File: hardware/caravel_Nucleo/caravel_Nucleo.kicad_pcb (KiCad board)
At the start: 2 copper layers, 67 x 92.4 mm, 80 parts, among them J1 USB_B_Micro - 10118193-0001LF, J10 Conn_01x09_Female, J2 Conn_01x02_Female, J3 Conn_01x02_Male, J4 Conn_01x04_Female, J5 Conn_01x02_Male, J6 Conn_01x02_Male, J7 Conn_01x06_Female, J8 Conn_01x03, J9 Conn_01x03, SW1 SW_Push - SKQGADE010, T1 Logo, T2 Logo, U1 FT232H, U10 MCP4661, U11 NUCLEO144-F429ZI, U2 SN74LVC1G125DCKR, U3 SN74LVC1G125DCKR, U4 MCP1319MT-29LE-OT, U5 TAR5SxxU_SOT353F, U6 TAR5SxxU_SOT353F, U7 W25Q32FVSS, U8 caravel_breakout, U9 MIC2211-AAYML-TR, X1 DSC6001_10MHZ, Y1 CSTNE12M0GH5L000R0

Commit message: [in review] update caravel board Nucleo-144 hat
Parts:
- added J11: Conn_01x03, Connector_PinHeader_2.54mm:PinHeader_1x03_P2.54mm_Vertical, F.Cu at (146.9, 123.0)
- moved T2 52.3 mm to (109.0, 144.6)
- moved T1 51.8 mm to (109.0, 149.0)
- moved J5 3.95 mm to (108.7, 95.3), turned to 0 degrees
- moved D4 3.37 mm to (119.9, 151.3)
- moved R14 3.37 mm to (124.2, 151.3)
- moved J9 1.77 mm to (108.7, 89.9)
- moved X1 1.29 mm to (150.8, 104.9)
- moved J6 1.29 mm to (146.2, 104.9)
- moved J3 0.51 mm to (148.3, 138.7)
- moved D1 0.51 mm to (141.4, 98.2)
- moved D2 0.51 mm to (138.9, 98.2)
- moved R5 0.41 mm to (153.5, 74.7)
- moved R6 0.41 mm to (151.4, 74.7)
- moved C3 0.28 mm to (152.0, 91.3)
- moved C2 0.28 mm to (151.9, 89.1)
- renumbered R12 to R11, R13 to R12, R11 to R13
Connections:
- J10 pad 9: TIM3_CH2 -> xclk
- J3 pad 2: vccd1 -> vccd
- J4 pad 2: UART3_TX -> UART8_TX
- J4 pad 3: UART3_RX -> UART8_RX
- J5 pad 2: vddio -> vdda
- U1 pad 13: USB_SCK_TXD -> SPI5_SCK
- U1 pad 14: USB_SO_RXD -> SPI5_MISO
- U1 pad 15: USB_SI -> SPI5_MOSI
- U1 pad 16: USB_CS1 -> SPI5_CS
- U11 pad 1: UART3_TX -> unconnected-(U11-Pad1)
- U11 pad 136: unconnected-(U11-Pad136) -> UART8_RX
- U11 pad 2: UART3_RX -> unconnected-(U11-Pad2)
- U11 pad 29: unconnected-(U11-Pad29) -> PH0
- U11 pad 61: unconnected-(U11-Pad61) -> UART8_TX
- U2 pad 2: UART3_RX -> UART8_RX
- U2 pad 4: USB_SO_RXD -> SPI5_MISO
- U3 pad 2: USB_SCK_TXD -> SPI5_SCK
- U3 pad 4: UART3_TX -> UART8_TX
- U8 pad 36: UART3_RX -> UART8_RX
- U8 pad 37: UART3_TX -> UART8_TX
- U8 pad 38: USB_SCK_TXD -> SPI5_SCK
- U8 pad 39: USB_CS1 -> SPI5_CS
- U8 pad 40: USB_SO_RXD -> SPI5_MISO
- U8 pad 41: USB_SI -> SPI5_MOSI
- U8 pad 43: vccd1 -> vccd
- U8 pad 52: TIM3_CH2 -> xclk
- U8 pad 55: vddio -> vdda
- U8 pad 7: vddio -> vdda
- X1 pad 3: TIM3_CH2 -> xclk
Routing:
- net vdda: track 125.8 -> 328.0 mm, vias 8 -> 19
- net vccd: track 0.00 -> 142.7 mm, vias 0 -> 6
- net UART8_RX: track 0.00 -> 140.3 mm, vias 0 -> 5
- net SPI5_SCK: track 0.00 -> 132.6 mm, vias 0 -> 5
- net ~{RST}: track 15.6 -> 146.6 mm, vias 0 -> 2
- net SPI5_MISO: track 0.00 -> 130.2 mm, vias 0 -> 6
- net UART8_TX: track 0.00 -> 129.5 mm, vias 0 -> 5
- net GND: track 54.1 -> 174.2 mm, vias 9 -> 38
- net SPI5_CS: track 0.00 -> 114.8 mm, vias 0 -> 4
- net SPI5_MOSI: track 0.00 -> 99.4 mm, vias 0 -> 3
- net mprj_io[29]: track 0.00 -> 75.3 mm, vias 0 -> 2
- net mprj_io[28]: track 0.00 -> 73.7 mm
- net xclk: track 0.00 -> 71.9 mm, vias 0 -> 3
- net mprj_io[31]: track 0.00 -> 71.9 mm, vias 0 -> 2
- net mprj_io[30]: track 0.00 -> 70.1 mm, vias 0 -> 2
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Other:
- board size 67 x 92.4 mm -> 68.1 x 92.5 mm
- board text added: "5V"
- board text added: "CSB"
- board text added: "D0"
- board text added: "D1"
- board text added: "HAT"
- board text added: "IO[0]"
- board text added: "IO[10]"
- board text added: "IO[11]"
- board text added: "IO[12]"
- board text added: "IO[13]"
- board text added: "IO[14]"
- board text added: "IO[15]"
- board text added: "IO[16]"
- board text added: "IO[17]"
- board text added: "IO[18]"
- board text added: "IO[19]"
- board text added: "IO[1]"
- board text added: "IO[20]"
- board text added: "IO[21]"
- board text added: "IO[22]"
- board text added: "IO[23]"
- board text added: "IO[24]"
- board text added: "IO[25]"
- board text added: "IO[26]"
- board text added: "IO[27]"
- board text added: "IO[28]"
- board text added: "IO[29]"
- board text added: "IO[2]"
- board text added: "IO[30]"
- board text added: "IO[31]"
- board text added: "IO[32]"
- board text added: "IO[33]"
- board text added: "IO[34]"
- board text added: "IO[35]"
- board text added: "IO[36]"
- board text added: "IO[37]"
- board text added: "IO[3]"
- board text added: "IO[4]"
- board text added: "IO[5]"
- board text added: "IO[6]"
- board text added: "IO[7]"
- board text added: "IO[8]"
- board text added: "IO[9]"
- board text added: "MAIN"
- board text added: "MCO_8MHz"
- board text added: "N"
- board text added: "PH0"
- board text added: "SCL"
- board text added: "SDA"
- board text added: "TIM3_2"
- board text added: "TIM3_PWM"

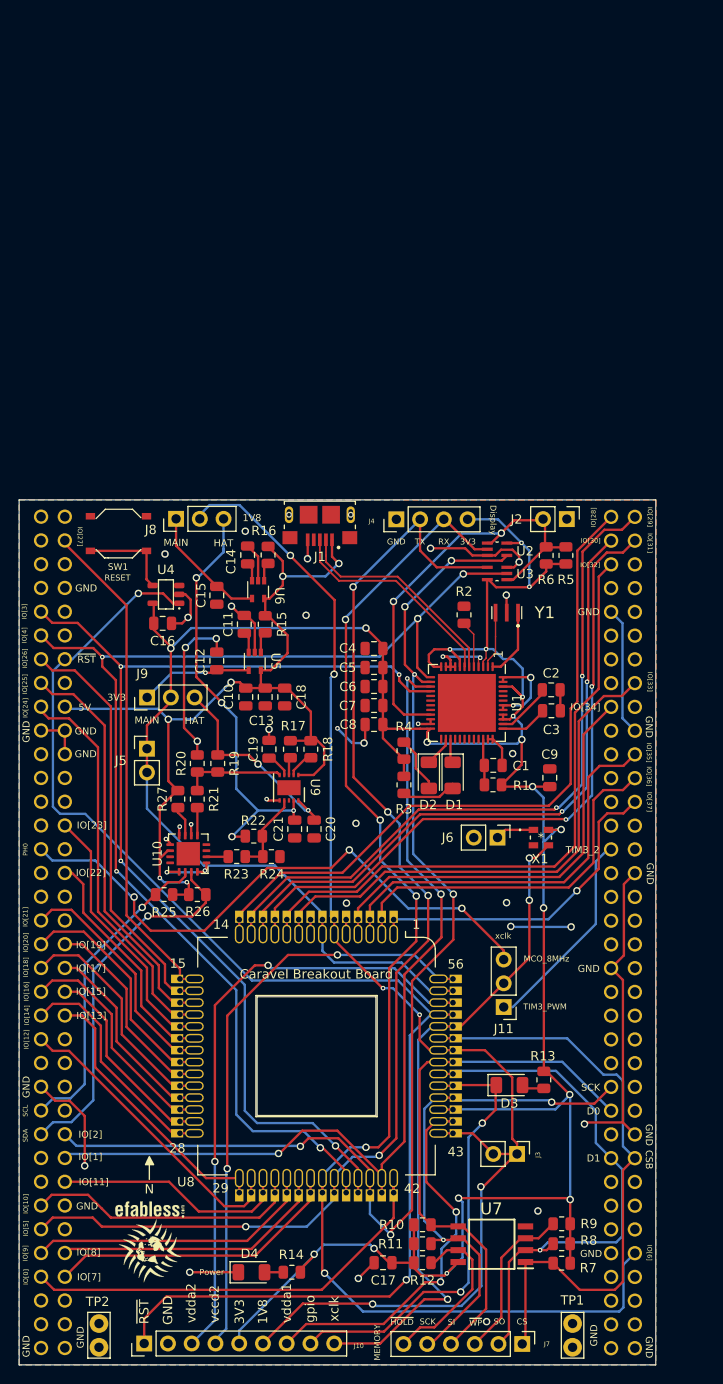
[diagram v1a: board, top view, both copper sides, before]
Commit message: update caravel board Nucleo-144 hat
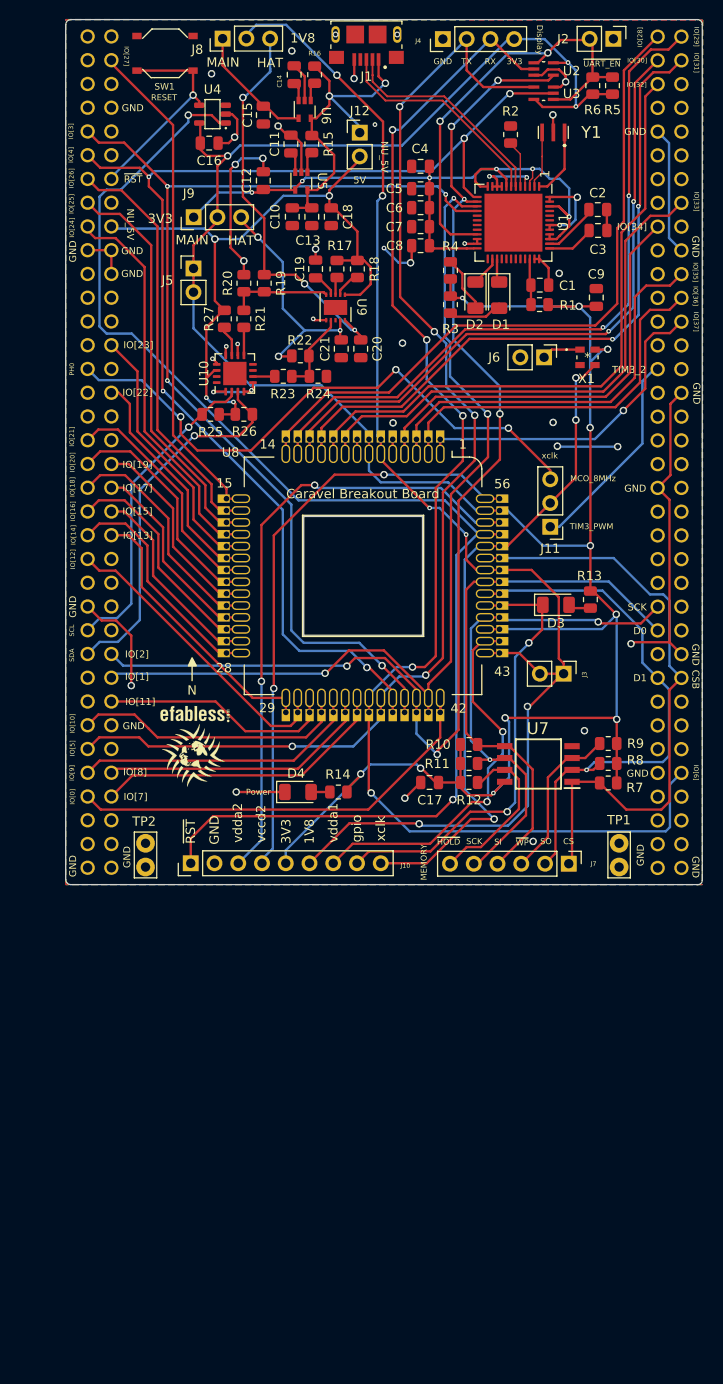
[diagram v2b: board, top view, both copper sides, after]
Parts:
- added J12: Conn_01x02_Male, Connector_PinHeader_2.54mm:PinHeader_1x02_P2.54mm_Vertical, F.Cu at (131.5, 29.5)
- moved T2 53.2 mm to (113.8, 91.6)
- moved T1 53.2 mm to (113.6, 96.1)
- moved C4 51.8 mm to (138.0, 33.1)
- moved R12 51.6 mm to (143.2, 99.0)
- moved C13 51.6 mm to (126.3, 38.5)
- moved C17 51.6 mm to (138.9, 99.0)
- moved C18 51.6 mm to (128.4, 38.5)
- moved D3 51.6 mm to (152.5, 80.0)
- moved J10 51.6 mm to (113.4, 107.6)
- moved U7 51.6 mm to (150.6, 97.0)
- moved C10 51.6 mm to (124.3, 38.5)
- moved C15 51.6 mm to (121.2, 27.6)
- moved C20 51.6 mm to (131.6, 52.6)
- moved C21 51.6 mm to (129.5, 52.6)
- moved J1 51.6 mm to (132.2, 19.0)
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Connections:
- net UART_EN renamed ~{UART_EN}
- C18 pad 2: +5V -> NU_5V
- C4 pad 2: vdda -> V3.3
- C5 pad 2: vdda -> V3.3
- C6 pad 2: vdda -> V3.3
- C7 pad 2: vdda -> V3.3
- C8 pad 2: vdda -> V3.3
- J8 pad 3: VOUT2 -> VOUT1
- J9 pad 3: VOUT1 -> VOUT2
- R17 pad 2: +5V -> NU_5V
- R18 pad 2: +5V -> NU_5V
- R25 pad 1: +5V -> NU_5V
- R26 pad 1: +5V -> NU_5V
- R27 pad 2: +5V -> NU_5V
- U1 pad 12: vdda -> V3.3
- U1 pad 24: vdda -> V3.3
- U1 pad 3: vdda -> V3.3
- U1 pad 39: vdda -> V3.3
- U1 pad 40: vdda -> V3.3
- U1 pad 46: vdda -> V3.3
- U1 pad 8: vdda -> V3.3
- U10 pad 14: +5V -> NU_5V
- U11 pad 14: ~{RST} -> ~{MR}
- U11 pad 18: +5V -> NU_5V
- U9 pad 1: +5V -> NU_5V
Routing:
- net NU_5V: track 0.00 -> 74.5 mm, vias 0 -> 4
- net V3.3: track 12.1 -> 77.9 mm, vias 1 -> 6
- net +5V: track 97.3 -> 36.8 mm, vias 6 -> 2
- net vdda: track 328.0 -> 290.4 mm, vias 19 -> 14
- net VOUT2: track 46.9 -> 26.3 mm, vias 4 -> 3
- net VOUT1: track 22.1 -> 42.8 mm, vias 2 -> 3
- net ~{MR}: track 9.97 -> 22.6 mm, vias 0 -> 1
- net GND: track 174.2 -> 167.6 mm, vias 38 -> 37
- net ~{UART_EN}: track 47.5 -> 48.6 mm
- net SPI5_MOSI: track 99.4 -> 100.2 mm
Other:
- outline, holes or cut-outs redrawn
- board text added: "NU_5V"
- board text added: "~{UART_EN}"

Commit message: update caravel nucleo hat board Rev A
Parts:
- removed TP2: TestPoint, TestPoint:TestPoint_Bridge_Pitch2.54mm_Drill1.0mm
- added C22: 1uf - CC0805KKX5R8BB105, Capacitor_SMD:C_0805_2012Metric, F.Cu at (138.0, 43.7)
- added C23: 0.01uf - CC0805KRX7R9BB103, Capacitor_SMD:C_0805_2012Metric, F.Cu at (135.1, 51.8)
- added C24: 10uf - CC0805KKX5R8BB106, Capacitor_SMD:C_0805_2012Metric, F.Cu at (138.0, 51.0)
- added R28: 10k, Resistor_SMD:R_0805_2012Metric, F.Cu at (138.0, 45.8)
- added R29: 0, Resistor_SMD:R_0805_2012Metric, F.Cu at (153.2, 76.7)
- added R30: 0, Resistor_SMD:R_0805_2012Metric, F.Cu at (159.7, 76.7)
- added R31: 0, Resistor_SMD:R_0805_2012Metric, F.Cu at (158.7, 86.0)
- added R32: 0, Resistor_SMD:R_0805_2012Metric, F.Cu at (153.2, 74.6)
- added U11: TAR5SxxU_SOT353F, Caravel_Board:SOT-353F, F.Cu at (138.0, 48.4)
- J10: value Conn_01x09_Female -> Conn_01x11_Female; footprint Connector_PinHeader_2.54mm:PinHeader_1x09_P2.54mm_Vertical -> Connector_PinHeader_2.54mm:PinHeader_1x11_P2.54mm_Vertical
- moved J10 5.09 mm to (108.3, 107.6)
- moved J11 2.24 mm to (154.1, 71.6)
- moved J3 2.16 mm to (154.3, 89.2)
- renumbered U11 to U12
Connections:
- C16 pad 2: vdda -> vddio
- C17 pad 1: vdda -> vddio
- C4 pad 2: V3.3 -> FTDI_V3.3
- C5 pad 2: V3.3 -> FTDI_V3.3
- C6 pad 2: V3.3 -> FTDI_V3.3
- C7 pad 2: V3.3 -> FTDI_V3.3
- C8 pad 2: V3.3 -> FTDI_V3.3
- C9 pad 2: vdda -> vddio
- J10 pad 2: GND -> vccd2
- J10 pad 3: vdda2 -> vccd
- J10 pad 4: vccd2 -> vccd
- J10 pad 5: vdda -> vccd
- J10 pad 6: vccd -> vdda2
- J10 pad 7: vdda1 -> vddio
- J10 pad 8: gpio -> vddio
- J10 pad 9: xclk -> vdda1
- J4 pad 4: vdda -> vddio
- J5 pad 1: vdda -> vddio
- J5 pad 2: vdda -> vddio
- J9 pad 2: vdda -> vddio
- R1 pad 2: vdda -> FTDI_V3.3
- R10 pad 2: vdda -> vddio
- R11 pad 2: vdda -> vddio
- R12 pad 2: vdda -> vddio
- R13 pad 1: vdda -> vddio
- R14 pad 1: vdda -> vddio
- R15 pad 1: Net-(R15-Pad1) -> EN_V3.3
- R16 pad 1: Net-(R16-Pad1) -> EN_V1.8
- R17 pad 1: Net-(R17-Pad1) -> EN_VOUT2
- R18 pad 1: Net-(R18-Pad1) -> EN_VOUT1
- R3 pad 2: vdda -> FTDI_V3.3
- R4 pad 2: vdda -> FTDI_V3.3
- R5 pad 1: vdda -> vddio
- R6 pad 1: vdda -> vddio
- R7 pad 2: vdda -> vddio
- R8 pad 2: vdda -> vddio
- R9 pad 2: vdda -> vddio
- U1 pad 12: V3.3 -> FTDI_V3.3
- U1 pad 24: V3.3 -> FTDI_V3.3
- U1 pad 25: unconnected-(U1-Pad25) -> ~{MR}
- U1 pad 29: unconnected-(U1-Pad29) -> EN_V1.8
- U1 pad 3: V3.3 -> FTDI_V3.3
- U1 pad 30: unconnected-(U1-Pad30) -> EN_V3.3
- U1 pad 39: V3.3 -> FTDI_V3.3
- U1 pad 40: V3.3 -> FTDI_V3.3
- U1 pad 46: V3.3 -> FTDI_V3.3
- U1 pad 8: V3.3 -> FTDI_V3.3
- U12 pad 121: Caravel_SCK -> SPI4_SCK
- U12 pad 123: Caravel_D0 -> SPI4_MOSI
- U12 pad 127: Caravel_D1 -> SPI4_MISO
- U12 pad 128: Caravel_CSB -> SPI4_CS
- U12 pad 14: ~{MR} -> unconnected-(U12-Pad14)
- U12 pad 21: unconnected-(U11-Pad21) -> EN_VOUT1
- U12 pad 23: unconnected-(U11-Pad23) -> EN_VOUT2
- U12 pad 3: unconnected-(U11-Pad3) -> ~{MR}
- U2 pad 5: vdda -> vddio
- U3 pad 5: vdda -> vddio
- U4 pad 5: vdda -> vddio
- U5 pad 1: Net-(R15-Pad1) -> EN_V3.3
- U6 pad 1: Net-(R16-Pad1) -> EN_V1.8
- U7 pad 8: vdda -> vddio
- U8 pad 45: vdda -> vddio
- U8 pad 55: vdda -> vddio
- U8 pad 7: vdda -> vddio
- U9 pad 2: Net-(R18-Pad1) -> EN_VOUT1
- U9 pad 3: Net-(R17-Pad1) -> EN_VOUT2
- X1 pad 4: vdda -> vddio
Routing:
- net vdda: track 290.4 -> 0.00 mm, vias 14 -> 0
- net vddio: track 0.00 -> 282.0 mm, vias 0 -> 13
- net FTDI_V3.3: track 0.00 -> 77.4 mm, vias 0 -> 6
- net vccd: track 142.8 -> 214.6 mm, vias 6 -> 10
- net V3.3: track 77.9 -> 12.1 mm, vias 6 -> 1
- net ~{MR}: track 22.6 -> 69.3 mm, vias 1 -> 2
- net EN_V1.8: track 0.00 -> 43.7 mm, vias 0 -> 2
- net EN_V3.3: track 0.00 -> 35.7 mm, vias 0 -> 2
- net EN_VOUT1: track 0.00 -> 34.0 mm, vias 0 -> 2
- net EN_VOUT2: track 0.00 -> 30.7 mm, vias 0 -> 2
- net +5V: track 36.8 -> 64.0 mm, vias 2 -> 4
- net SPI4_CS: track 0.00 -> 25.9 mm, vias 0 -> 1
- net SPI4_MISO: track 0.00 -> 12.3 mm
- net Caravel_D0: track 58.7 -> 46.5 mm, vias 0 -> 1
- net SPI4_MOSI: track 0.00 -> 12.2 mm, vias 0 -> 1
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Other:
- board text added: "EN_V1"
- board text added: "EN_V2"
- board text added: "NUCLEO HAT Rev A"
- board text added: "vccd1"
- board text added: "~{MR}"
- board text removed: "CS"

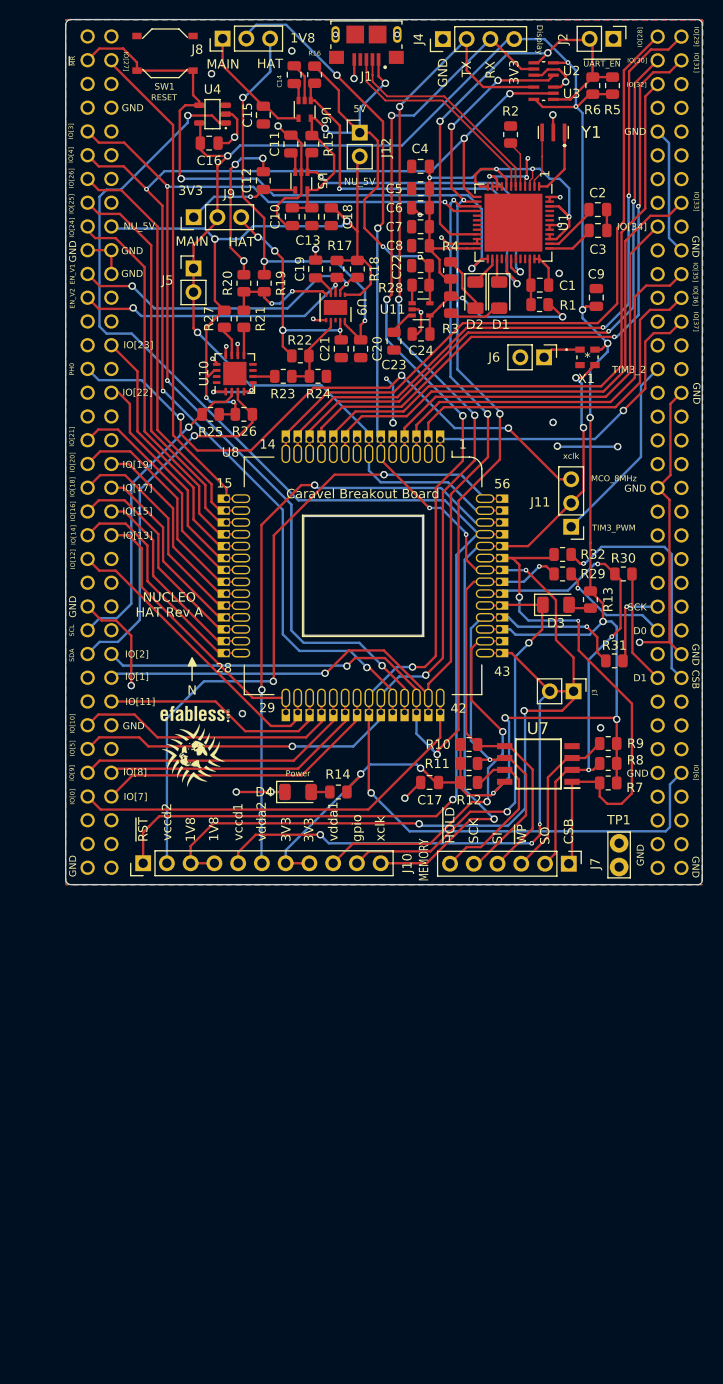
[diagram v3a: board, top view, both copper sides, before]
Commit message: update caravel nucleo hat board Rev A PCB
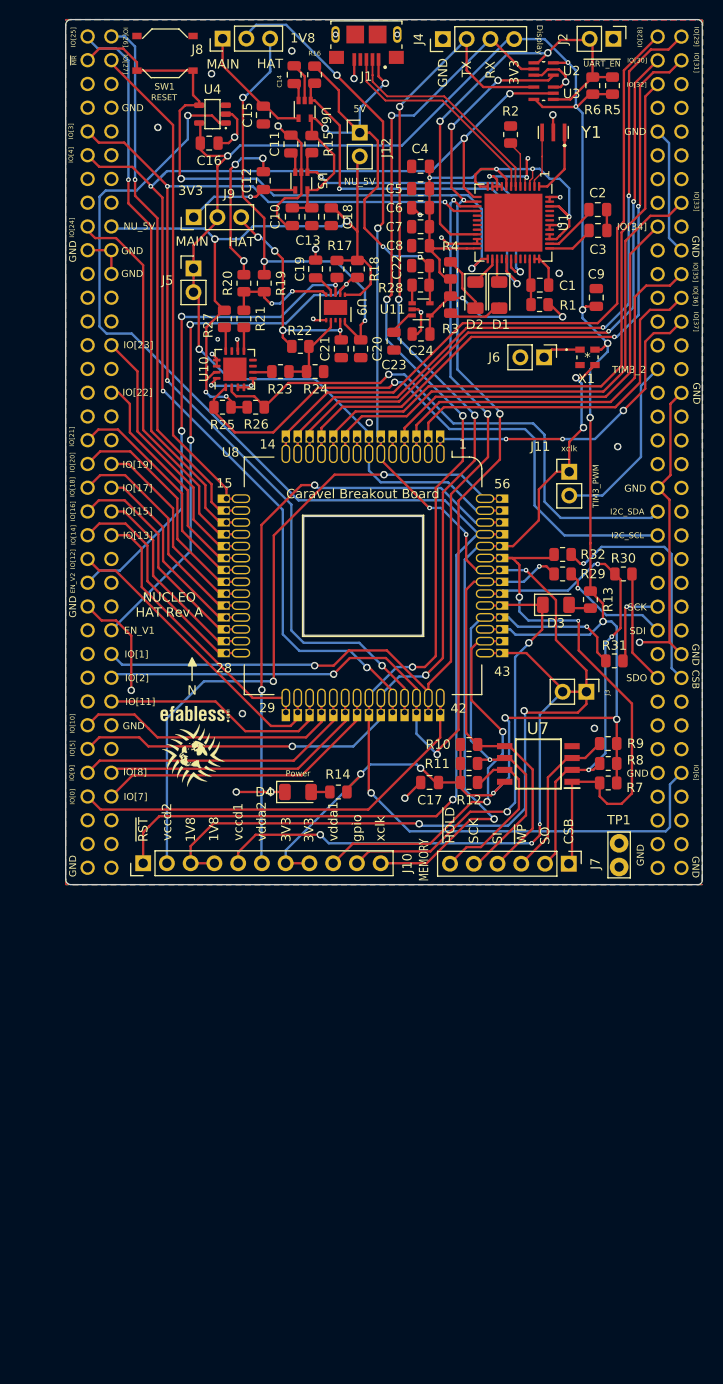
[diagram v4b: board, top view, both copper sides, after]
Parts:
- J11: value Conn_01x03 -> Conn_01x02; footprint Connector_PinHeader_2.54mm:PinHeader_1x03_P2.54mm_Vertical -> Connector_PinHeader_2.54mm:PinHeader_1x02_P2.54mm_Vertical
- U12: value NUCLEO144-F429ZI -> NUCLEO144-F746ZG
- moved J11 5.89 mm to (153.9, 65.7), turned to 0 degrees
- moved R26 1.48 mm to (120.3, 58.8)
- moved R25 1.48 mm to (116.8, 58.8)
- moved J3 1.37 mm to (155.7, 89.3)
- moved R22 1.02 mm to (125.1, 52.3)
- moved R23 0.59 mm to (123.0, 55.0)
- moved R24 0.59 mm to (126.7, 55.0)
- moved U10 0.46 mm to (118.1, 54.8)
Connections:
- net vddio renamed vdda
- J11 pad 1: TIM3_CH2 -> xclk
- J11 pad 2: xclk -> TIM3_CH2
- R25 pad 2: I2C2_SCL -> I2C4_SCL
- R26 pad 2: I2C2_SDA -> I2C4_SDA
- U1 pad 14: SPI5_MISO -> SPI5_MOSI
- U1 pad 15: SPI5_MOSI -> SPI5_MISO
- U10 pad 1: GND -> I2C4_SCL
- U10 pad 11: Net-(R27-Pad1) -> unconnected-(U10-Pad11)
- U10 pad 12: GND -> Net-(R27-Pad1)
- U10 pad 14: NU_5V -> GND
- U10 pad 15: (no net) -> NU_5V
- U10 pad 16: (no net) -> GND
- U10 pad 2: I2C2_SCL -> I2C4_SDA
- U10 pad 3: I2C2_SDA -> GND
- U12 pad 1: unconnected-(U12-Pad1) -> mprj_io[25]
- U12 pad 113: unconnected-(U12-Pad113) -> I2C4_SDA
- U12 pad 115: unconnected-(U12-Pad115) -> I2C4_SCL
- U12 pad 13: mprj_io[26] -> unconnected-(U12-Pad13)
- U12 pad 15: mprj_io[25] -> unconnected-(U12-Pad15)
- U12 pad 2: unconnected-(U12-Pad2) -> mprj_io[26]
- U12 pad 21: EN_VOUT1 -> unconnected-(U12-Pad21)
- U12 pad 23: EN_VOUT2 -> unconnected-(U12-Pad23)
- U12 pad 29: PH0 -> unconnected-(U12-Pad29)
- U12 pad 47: unconnected-(U12-Pad47) -> EN_VOUT2
- U12 pad 51: I2C2_SCL -> unconnected-(U12-Pad51)
- U12 pad 52: unconnected-(U12-Pad52) -> EN_VOUT1
- U12 pad 53: I2C2_SDA -> unconnected-(U12-Pad53)
- U2 pad 4: SPI5_MISO -> SPI5_MOSI
- U8 pad 40: SPI5_MISO -> SPI5_MOSI
- U8 pad 41: SPI5_MOSI -> SPI5_MISO
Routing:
- net I2C4_SCL: track 0.00 -> 64.7 mm, vias 0 -> 1
- net PH0: track 64.3 -> 0.00 mm, vias 3 -> 0
- net I2C4_SDA: track 0.00 -> 59.0 mm, vias 0 -> 1
- net I2C2_SDA: track 40.0 -> 0.00 mm, vias 1 -> 0
- net I2C2_SCL: track 33.8 -> 0.00 mm, vias 1 -> 0
- net SPI5_MOSI: track 99.4 -> 130.8 mm, vias 3 -> 6
- net SPI5_MISO: track 130.2 -> 99.6 mm, vias 6 -> 3
- net EN_VOUT1: track 34.0 -> 57.6 mm, vias 2 -> 3
- net EN_VOUT2: track 30.7 -> 53.7 mm, vias 2 -> 3
- net mprj_io[25]: track 43.6 -> 61.2 mm, vias 0 -> 1
- net mprj_io[26]: track 45.0 -> 58.6 mm, vias 0 -> 1
- net GND: track 179.3 -> 168.2 mm, vias 38 -> 36
- net vccd: track 214.6 -> 218.9 mm
- net NU_5V: track 78.5 -> 77.3 mm
- net TIM3_CH2: track 20.7 -> 19.5 mm
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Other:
- board text added: "I2C_SCL"
- board text added: "I2C_SDA"
- board text added: "SDI"
- board text added: "SDO"
- board text removed: "D0"
- board text removed: "D1"
- board text removed: "MCO_8MHz"
- board text removed: "PH0"
- board text removed: "SCL"
- board text removed: "SDA"
